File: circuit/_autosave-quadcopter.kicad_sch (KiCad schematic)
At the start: 121 parts, among them J1 Conn_01x01_Female, J10 Conn_01x01_Female, J12 Conn_01x01_Female, J13 Conn_01x01_Female, J15 Conn_01x01_Female, J16 Conn_01x01_Female, J17 Conn_01x01_Female, J18 USB_C_Receptacle_USB2.0, J19 Conn_01x08_Male, J2 Conn_01x01_Female, J21 Conn_01x01_Female, J22 Conn_01x01_Female, J23 Conn_01x01_Female, J24 Conn_01x01_Female, J25 Conn_01x01_Female, J26 Conn_01x01_Female, J28 Conn_01x01_Female, J29 Conn_01x01_Female, J3 Conn_01x01_Female, J30 Conn_01x01_Female, J31 Conn_01x01_Female, J32 Conn_01x01_Female, J33 Conn_01x01_Female, J34 Conn_01x01_Female, J37 Conn_01x01_Female, J38 Conn_01x01_Female, J39 Conn_01x01_Female, J40 Conn_01x01_Female, J41 Conn_01x01_Female, J42 Conn_01x01_Female, J43 Conn_01x01_Female, J44 Conn_01x01_Female, J45 Conn_01x01_Female, J46 Conn_01x01_Female, J47 Conn_01x01_Female, J48 Conn_01x01_Female, J49 Conn_01x01_Female, J5 Conn_Coaxial, J50 Conn_01x01_Female, J6 Conn_01x06_Male, J7 Conn_01x01_Female, J8 Conn_01x01_Female, J9 Conn_01x01_Female, Q1 AO3400A, SW1 SW_DIP_x01, U1 STM32G431CBU6, U2 ICM-42605, U3 DPS310, U4 3V3, U5 5V out, 30V max, U6 AT7456E, U7 W25Q128JVS, U8 SX1281, Y1 16M, Y2 27M

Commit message: Basic layout for OSD-less MCU in progress
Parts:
- removed C19, C20, C21, C22: 100n, Capacitor_SMD:C_0402_1005Metric, symbol Device:C
- removed C24, C25: 47u, Capacitor_SMD:C_0805_2012Metric, symbol Device:C
- removed J12: Conn_01x01_Female, TestPoint:TestPoint_Pad_1.5x1.5mm, symbol Connector:Conn_01x01_Female
- removed R10, R11: 75, Resistor_SMD:R_0402_1005Metric, symbol Device:R
- removed R7, R8, R9: 1k, Resistor_SMD:R_0402_1005Metric, symbol Device:R
- removed U6: AT7456E, Package_SO:TSSOP-28_4.4x9.7mm_P0.65mm, symbol Anyleaf_Shared:AT7456E
- removed Y2: 27M, Oscillator:Oscillator_SMD_EuroQuartz_XO32-4Pin_3.2x2.5mm, symbol Device:Crystal_GND24
- C31, F1, L1: now in the parts list
- J50: footprint TestPoint:TestPoint_Pad_1.0x1.0mm -> TestPoint:TestPoint_Pad_2.0x2.0mm
- L2: value 100u -> 100u 450mA
- U7: value W25Q128JVS -> W25Q80DVUXIE TR; Digikey (none) -> W25Q80DVUXIETR-ND
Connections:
- net +3V3: now also L1.1; no longer C1.2, C3.2, C4.1, U2.5 (VDDIO), U2.8 (VDD)
- net MISO_2: now also U7.2 (DO(IO1))
- net MISO_3: no longer U7.2 (DO(IO1))
- net MOSI_2: now also U7.5 (DI(IO0))
- net MOSI_3: no longer U7.5 (DI(IO0))
- net SCK_2: now also U7.6 (CLK)
- net SCK_3: no longer U7.6 (CLK)
- net IMU_pwr: now reaches C31.2, L1.2
- net IMU_pwr: now also C1.2, C3.2, C4.1, U2.5 (VDDIO), U2.8 (VDD)
- net at F1.1: now also D1.2 (A)
- net at F1.2: now also J18.A4 (VBUS), J18.A9 (VBUS), J18.B4 (VBUS), J18.B9 (VBUS)
- no-connect marks 13 -> 11
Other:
- note added: "todo: Higher capacity flash"
- note added: "todo: Xtal connection on SX1280! If not, does/can it get clock from MCU?"
- note removed: ""No external load capacitors are needed""
- note removed: "Header to connect to Rx, and VTX."
- note removed: "LDO voltage too low. Try again!"
- note removed: "Note: This cap is expensive, but is a smaller footprint than others of this cap"
- note removed: "On screen display (Analog)"
- note removed: "See the MAX7456 datasheet for info on choosing C_OUT and C_SAG capacitors. Larger cap values result in lower distortion. (But may be bulkier)"
- note removed: "todo: Check voltage req of C_x caps. Currently at 6v. Use 1206 for 10v"
- note removed: "todo: Xtal connection on SX1280? If not, does/can it get clock from MCU?"
- moved on the sheet: C14, C15, C27, C31, D2, F1, J19, L1, L2, U5

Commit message: More work on PCB
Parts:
- removed J38, J39: Conn_01x01_Female, TestPoint:TestPoint_Pad_2.0x2.0mm, symbol Connector:Conn_01x01_Female
- added J4: Conn_01x01_Female, TestPoint:TestPoint_Pad_1.5x1.5mm, symbol Connector:Conn_01x01_Female
- L1: value 10u -> 100u 450mA; footprint Inductor_SMD:L_0603_1608Metric -> Anyleaf_Shared:SMNR4020 inductor; LCSC C1035 -> C467068
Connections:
- net VID_IN is gone; now on net +BATT: J6.6 (Pin_6)
- net +5V: no longer J26.1 (Pin_1), J6.5 (Pin_5)
- net +BATT: now also J25.1 (Pin_1); no longer J29.1 (Pin_1), J6.2 (Pin_2)
- net BATT_DIV: now also U1.12 (PA4); no longer U1.16 (PC4)
- net GND: now also J26.1 (Pin_1), J29.1 (Pin_1), J6.2 (Pin_2), J6.5 (Pin_5); no longer J25.1 (Pin_1), J28.1 (Pin_1), J6.1 (Pin_1), J6.4 (Pin_4)
- net IMU_INTERRUPT: now also U1.16 (PC4); no longer U1.12 (PA4)
- net UART1_RX: now also J28.1 (Pin_1), J6.3 (Pin_3)
- net UART1_TX: now also J13.1 (Pin_1), J6.4 (Pin_4)
- net UART2_RX: now also J6.1 (Pin_1), J4.1 (Pin_1)
- net VID_OUT: no longer J13.1 (Pin_1), J6.3 (Pin_3)
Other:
- note added: "(HDL / SBUS)"
- note added: "7-26V for both HD-zero and DJI, so can't use with 8S battery!"
- note added: "Digital camera/Vtx pins and pads. DJI layout. Hd-zero layout is GND, Pwr, Rx, Tx, (sometimes Smart Audio and/or SBUS?)"
- note removed: "Analog camera"
- note removed: "Analog vid transmitter"
- moved on the sheet: J13, J25, J26, J28, J29, J6

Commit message: Added filtering /decoupling circuitry to LoRa chip. More work on board routing
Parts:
- added C19: 10n, Capacitor_SMD:C_0402_1005Metric, symbol Device:C
- added C20: .8p (actual: 1pF), Capacitor_SMD:C_0402_1005Metric, symbol Device:C
- added C21, C24: 1.2p, Capacitor_SMD:C_0402_1005Metric, symbol Device:C
- added C22: 0.5p, Capacitor_SMD:C_0402_1005Metric, symbol Device:C
- added C25: 100p, Capacitor_SMD:C_0402_1005Metric, symbol Device:C
- added L3: 15u, Inductor_SMD:L_0805_2012Metric, symbol Device:L
- added L4: 3n, Inductor_SMD:L_0402_1005Metric, symbol Device:L
- added L5: 2.5n (3n actual), Inductor_SMD:L_0402_1005Metric, symbol Device:L
- added Y2: 52Mhz, 10pF, Crystal:Crystal_SMD_3225-4Pin_3.2x2.5mm, symbol Device:Crystal_GND24
- C26: value 100n -> 470n, 10V; LCSC C1525 -> C47339
- C28: value 100n -> 10n; LCSC C1525 -> C15195
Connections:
- net +3V3: now also C26.1, U8.12 (DCC_FB), L3.1; no longer C26.2, U8.1 (VR_PA), U8.11 (VBAT_IO), U8.15 (VBAT)
- net GND: now also C26.2, C19.1, C20.2, C21.2, C24.2, Y2.2, Y2.4; no longer C26.1
- net UART2_RX: no longer J4.1 (Pin_1)
- net UART2_TX: now also J4.1 (Pin_1)
- net V_DCC2: now reaches U8.14 (DCC_SW)
- net V_DCC2: now also L3.2
- net at U8.22 (RFIO): now also C20.1, L4.1; no longer J5.1 (In)
- net at U8.4 (XTA): now also Y2.1
- net at U8.6 (XTB): now also Y2.3
- new net: C21.1, C22.1, L4.2, L5.1
- new net: C22.2, C24.1, C25.1, L5.2
- new net: C19.2, U8.1 (VR_PA)
- new net: C25.2, J5.1 (In)
- no-connect marks 11 -> 7
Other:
- note added: "Note: Voltage range of CADDX vista DJI: 7.4 - 26.4V HDzero: Racev2: 7-26V Hdzero freestyle: 7-17V max (4S!)"
- note added: "Reference SX1280 Datsheet, section 15.1: Reference Design"
- note removed: "ESC (iflight-layout header)"
- note removed: "todo: Do we need rst?"
- note removed: "todo: Temporarily removed this IMU pwr filtering due to size"
- note removed: "todo: Xtal connection on SX1280! If not, does/can it get clock from MCU?"
- moved on the sheet: C2, C5, J5, U3

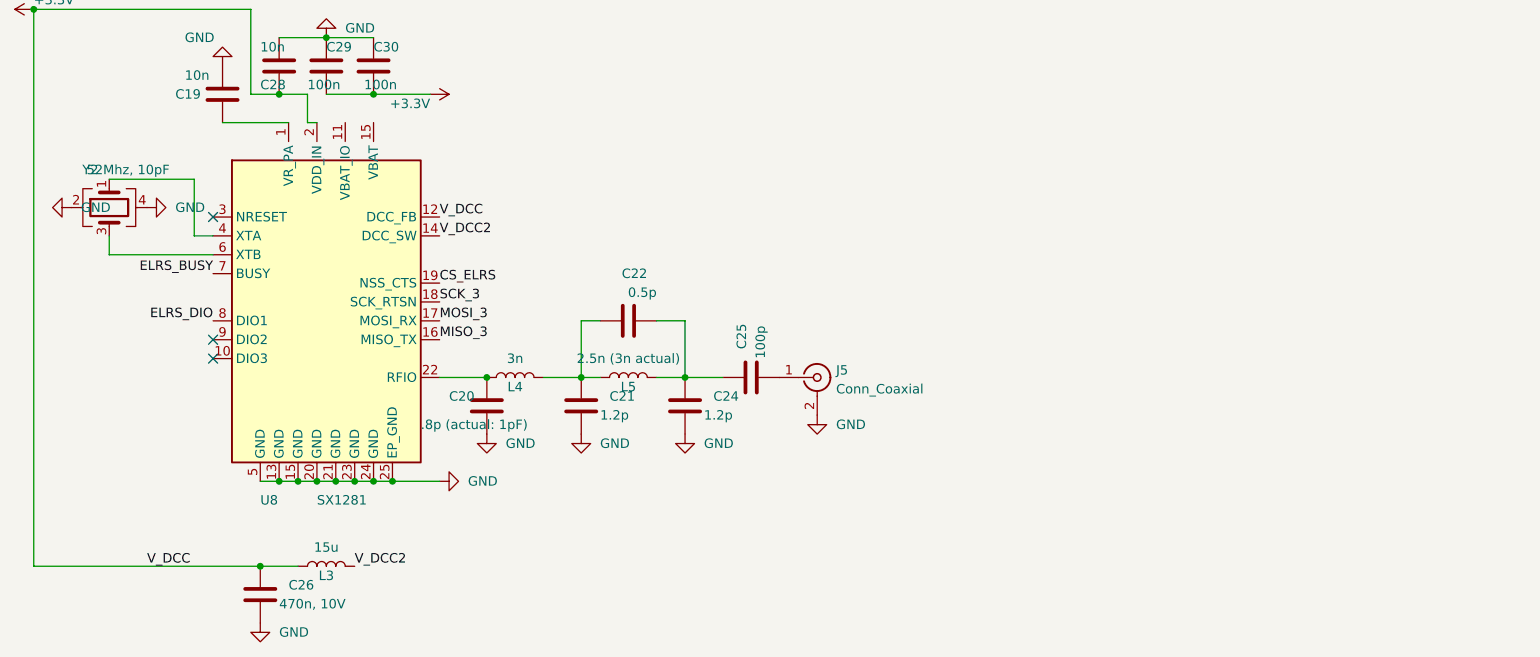
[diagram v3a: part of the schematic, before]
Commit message: replaced passive filter on RF with single IC
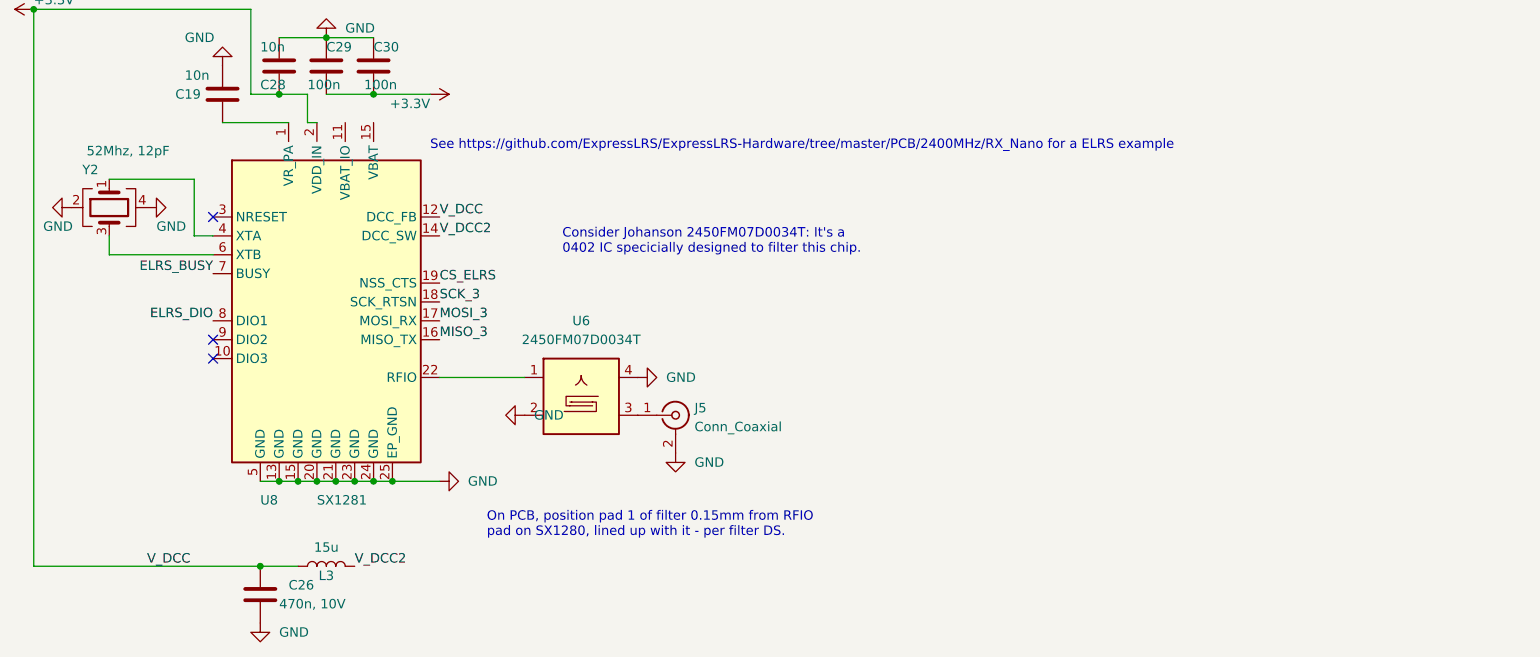
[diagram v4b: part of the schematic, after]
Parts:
- removed C20: .8p (actual: 1pF), Capacitor_SMD:C_0402_1005Metric, symbol Device:C
- removed C21, C24: 1.2p, Capacitor_SMD:C_0402_1005Metric, symbol Device:C
- removed C22: 0.5p, Capacitor_SMD:C_0402_1005Metric, symbol Device:C
- removed C25: 100p, Capacitor_SMD:C_0402_1005Metric, symbol Device:C
- removed L4: 3n, Inductor_SMD:L_0402_1005Metric, symbol Device:L
- removed L5: 2.5n (3n actual), Inductor_SMD:L_0402_1005Metric, symbol Device:L
- added U6: 2450FM07D0034T, Anyleaf_Shared:2450FM07D0034, symbol Filter:SAFFA1G58KA0F0A
- Y2: value 52Mhz, 10pF -> 52Mhz, 12pF; Digikey 2388-SXT32410AA07-52.000MT-ND -> FL520WFMT1TR-ND; Mouser (none) -> 729-FW520WFMT1
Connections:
- net GND: now also U6.2, U6.4, U6.5
- net at U8.22 (RFIO): now also U6.1
- net at J5.1 (In): now also U6.3
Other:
- note added: "Consider Johanson 2450FM07D0034T: It's a 0402 IC specicially designed to filter this chip."
- note added: "On PCB, position pad 1 of filter 0.15mm from RFIO pad on SX1280, lined up with it - per filter DS."
- note added: "See https://github.com/ExpressLRS/ExpressLRS-Hardware/tree/master/PCB/2400MHz/RX_Nano for a ELRS example"
- moved on the sheet: J5

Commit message: Adjusted connections and routing for ELRS power system
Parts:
- U7: value W25Q80DVUXIE TR -> W25Q80DVUXIE TR (16M)
- Y2: footprint Crystal:Crystal_SMD_3225-4Pin_3.2x2.5mm -> Crystal:Crystal_SMD_2016-4Pin_2.0x1.6mm
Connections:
- net +3V3: now also U8.11 (VBAT_IO), U8.15 (VBAT); no longer C26.1, C28.2, L3.1, U8.12 (DCC_FB), U8.2 (VDD_IN)
- net UART1_RX: now also J4.1 (Pin_1), J6.1 (Pin_1); no longer J28.1 (Pin_1), J6.3 (Pin_3)
- net UART1_TX: no longer J13.1 (Pin_1), J6.4 (Pin_4)
- net UART2_RX: now also J28.1 (Pin_1), J6.3 (Pin_3); no longer J43.1 (Pin_1), J6.1 (Pin_1)
- net UART2_TX: now also J13.1 (Pin_1), J6.4 (Pin_4); no longer J4.1 (Pin_1), J42.1 (Pin_1)
- net UART4_RX: now also J43.1 (Pin_1)
- net UART4_TX: now also J42.1 (Pin_1)
- new net V_DCC: C26.1, C28.2, L3.1, U8.12 (DCC_FB), U8.2 (VDD_IN)
- no-connect marks 7 -> 9
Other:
- note added: "(HDL / SA)"
- note added: "Note: DJI uses optional HDL (SBUS), which is Rx. HDzero uses optional Smart Audio, which is Tx. So, you have a choice"
- note removed: "(HDL / SBUS)"
- note removed: "todo: Higher capacity flash"
- moved on the sheet: C2, C23, C5, U3, U7

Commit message: More work on routing
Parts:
- added D4: SOD24-7 26V breakdown, Diode_SMD:D_SOD-323, symbol Device:D
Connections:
- net BAT_IN: now also D4.2 (A); no longer L2.1
- new net: D4.1 (K), L2.1
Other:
- note added: "10v reg for cam and vtx? Would allow for 8S batteries, if you also up max voltage on a few other parts"
- note added: "Example full buzzer circuit. Not on PCB or BOM."
- note added: "SWD connections for ST-Link debugging and flashing"
- note added: "TVS diode to block transient voltage spikes"
- note added: "Todo: Switching reg, 1A for U5"
- note added: "Todo: TVS diode across battery?"
- note added: "Using Diatone pinout, since it's perhaps the most popular (2022) Note that this places the battery line next to the signal pins; Batt -> Gnd -> current/uart -> motor may be a better layout."
- note added: "todo: Bigger flash, on back side?"
- note removed: "10v reg for cam and vtx?"
- note removed: "Example full buzzer circuit. Not on BOM!"
- note removed: "See https://github.com/ExpressLRS/ExpressLRS-Hardware/tree/master/PCB/2400MHz/RX_Nano for a ELRS example"
- note removed: "Using Diatone pinout, since it's perhaps the most popular (2022)"
- moved on the sheet: C7, C8, D3, J16, J17, J32, J33, J40, J41, J42, J43, J44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
